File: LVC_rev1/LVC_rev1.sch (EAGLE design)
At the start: 29 parts, among them T1 DMP4047SK3, T3 BSS84, T4 2N7002P, T6 2N7002P, U1 MIC5239-FIXED, U2 ATTINY84

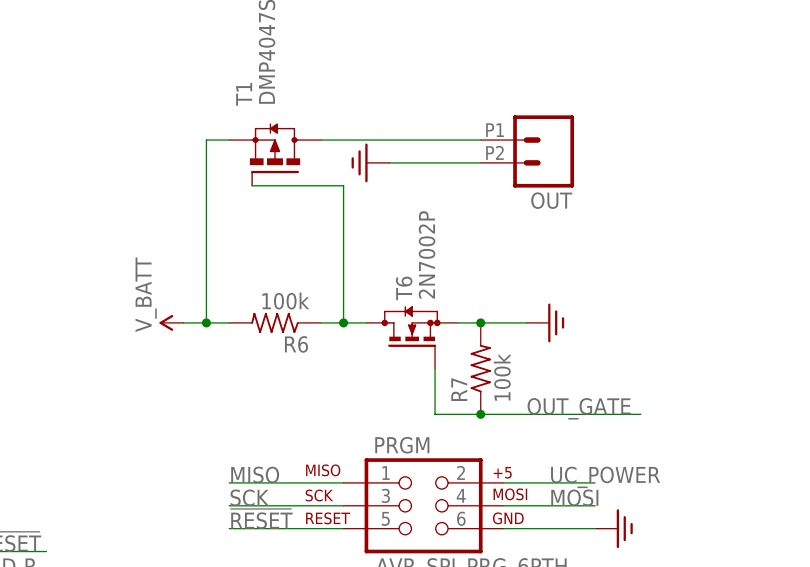
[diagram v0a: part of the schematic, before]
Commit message: Changed documentation error with T2
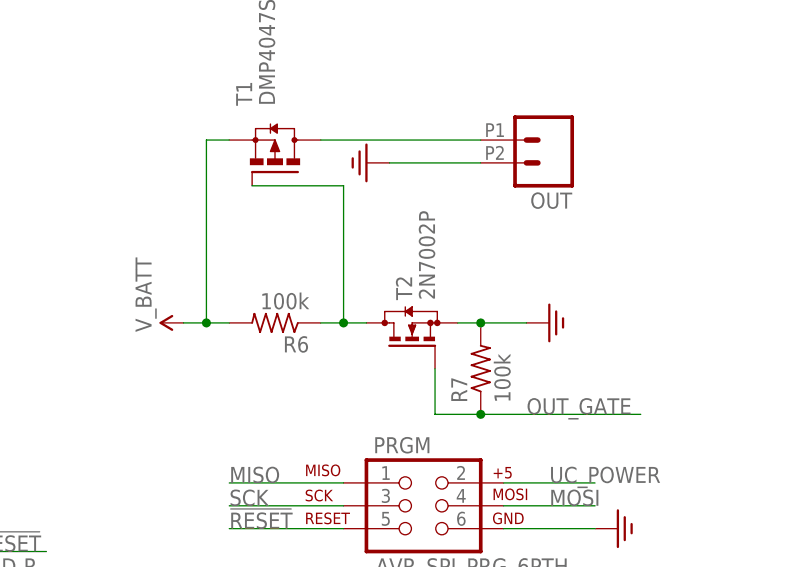
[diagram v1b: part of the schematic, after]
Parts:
- renumbered T6 to T2
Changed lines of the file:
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@@
 <part name="R13" library="rcl" deviceset="R-US_" device="R0603" value="100k"/>
 <part name="T4" library="transistor-small-signal" deviceset="2N7002P" device=""/>
-<part name="T6" library="transistor-small-signal" deviceset="2N7002P" device=""/>
+<part name="T2" library="transistor-small-signal" deviceset="2N7002P" device=""/>
 <part name="C3" library="rcl" deviceset="C-EU" device="C0603" value="0.1UF"/>
 </parts>
@@
 <instance part="R13" gate="G$1" x="99.06" y="66.04" rot="R270"/>
 <instance part="T4" gate="G$1" x="88.9" y="53.34"/>
-<instance part="T6" gate="G$1" x="203.2" y="144.78" rot="R90"/>
+<instance part="T2" gate="G$1" x="203.2" y="144.78" rot="R90"/>
 <instance part="C3" gate="G$1" x="33.02" y="96.52"/>
 </instances>
@@
 <junction x="210.82" y="144.78"/>
 <wire x1="210.82" y1="144.78" x2="208.28" y2="144.78" width="0.1524" layer="91"/>
-<pinref part="T6" gate="G$1" pin="S"/>
+<pinref part="T2" gate="G$1" pin="S"/>
 </segment>
 <segment>
@@
 <pinref part="R7" gate="G$1" pin="1"/>
 <wire x1="210.82" y1="134.62" x2="228.6" y2="134.62" width="0.1524" layer="91"/>
-<pinref part="T6" gate="G$1" pin="G"/>
+<pinref part="T2" gate="G$1" pin="G"/>
 <wire x1="205.74" y1="139.7" x2="205.74" y2="134.62" width="0.1524" layer="91"/>
 <wire x1="205.74" y1="134.62" x2="210.82" y2="134.62" width="0.1524" layer="91"/>
@@
 <pinref part="T1" gate="G$1" pin="G"/>
 <wire x1="195.58" y1="160.02" x2="185.42" y2="160.02" width="0.1524" layer="91"/>
-<pinref part="T6" gate="G$1" pin="D"/>
-</segment>
-</net>
+<pinref part="T2" gate="G$1" pin="D"/>
+</segment>
+</net>
